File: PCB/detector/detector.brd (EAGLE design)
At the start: 53.3 x 51.7 mm, 36 parts, among them IC1 STM32F042K6T6

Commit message: almost ready
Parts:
- removed +3.3V, +5V: (no value), con-ptr500:AK500/2
- removed D1: 3.3V, diode:SOD80C
- removed JP1: (no value), pinhead:1X03/90
- removed JP2: (no value), pinhead:1X04/90
- removed Q1: (no value), crystal:CTS406
- removed S1: DTSM-3, swtich:DTSM-3
- added BAT1: BAT_3V, battery CR1216:CR1216
- added C18, C23: 100nF, resistor:C0603
- added C19, C20, C21, C22: 22pF, resistor:C0603
- added C24: 1u, rcl:C0603
- added C25: 100p, rcl:C0603
- added C26: 100n, rcl:C0603
- added C27, C28: 1n, rcl:C0603
- added CAN+PWR: 4PIN_3.81_KATOWA, zielone raster 3.81:CON-PHOENIX_3.81-4PIN_KAT
- added CR1: 32,768kHz, crystal_scorpio:IL3X
- added D3_SK1: 5A, diode:DO214AA
- added DA1: SN65HVD230, can_driver:SO08
- added FUSE1: 3A, resistor:R0603
- added L1: 1uH/500mA, rcl:L2012C
- added L2: 10uH/20mA, rcl:L2012C
- added L3, L4: (no value), rcl:L3216C
- added LED1, LED3: zielona, led:CHIP-LED0603
- added LED2: niebieska, led:CHIP-LED0603
- added LED4: czerwona, led:CHIP-LED0603
- added MA_BYC_ACS711_!!: ACS712, acs712:SO08
- added PROGRAMATOR: (no value), pinhead:1X06
- added PRZETWORNICA1: 3.3V, OKI-78SR:TO220
- added R10: 120R*, resistor:R0603
- added R11: 390k, resistor:R0603
- added R12, R13: 10k, resistor:R0603
- added R14, R15, R16: 470R, resistor:R0603
- added TRANSIL1: 3.3V, diode:SMBJ
- added U$2: STM32F072RBT6, STM32F072RBT6:TQFP64
- added U$3: ABM3, crystal_scorpio:ABM3
- added U$6: LC03-6R2G, LC03-6R2 - diody ESD do magistrali:SOIC-8
- added U1: LT5538, DFN-8:DFN-8_3X3
- added U2: B39431B3710U410, SON120P300X300X110-6N:SON120P300X300X110-6N
- added ZW_MASY: (no value), resistor:R0603
- added ZW_ZASILANIA: (no value), pinhead:1X02
- C1: value 100n -> (none); device rcl:C0805 -> rcl:C0603
- C10, C12, C15: value 100n -> 100nF; device rcl:C0805 -> resistor:C0603
- C11, C9: value 4.7u -> 100nF; device rcl:CT3216 -> resistor:C0603
- C13: value 10n -> 100nF; device rcl:C0805 -> resistor:C0603
- C14: value 1u -> 100nF; device rcl:CT3216 -> resistor:C0603
- C16: value 20p -> 100nF; device rcl:C0805 -> resistor:C0603
- C17: value 20p -> 6,3V/100uF; device rcl:C0805 -> resistor:E2-5
- C2: value 100p -> 4,7uF; device rcl:C0805 -> rcl:SMC_A
- C3: value 100p -> (none); device rcl:C0805 -> rcl:C0603
- C4: device rcl:C0805 -> rcl:C0603
- C5, C6: value 100n -> 100p; device rcl:C0805 -> rcl:C0603
- C7: value 10u -> 4,7uF; device rcl:C0805 -> rcl:SMC_A
- C8: value 100n -> 1uF; device rcl:C0805 -> resistor:C0603
- IC1: value STM32F042K6T6 -> LM50; device STM32F042K6T6:QFP80P900X900X160-32N -> linear:SOT23
- R1: value 60.4R -> VARISTORCN0603; device rcl:R0805 -> varistor:CT/CN0603
- R2: value 2k -> (none); device rcl:R0805 -> rcl:R0603
- R3: value 301R -> 820R; device rcl:R0805 -> resistor:R0603
- R4: value 10k -> 56R; device rcl:R0805 -> rcl:R0603
- R5: value 20k -> (none); device rcl:R0805 -> rcl:R0603
- R6: value 1430R -> 10k; device rcl:R0805 -> resistor:R0603
- R7: value 3.74k -> 100K; device rcl:R0805 -> resistor:R0603
- R8: value 2k -> ZW 0-100K; device rcl:R0805 -> resistor:R0603
- R9: value 0R -> 32k; device rcl:R0805 -> resistor:R0603
- U$1: value ADL5902 -> TQP3M9036; device ADL5902:ADL5902 -> DFN-8:DFN-8_2X2
- moved C11 111.4 mm to (127.2, 23.7), flipped to the bottom
- moved C9 101.8 mm to (118.9, 18.9), flipped to the bottom, turned to 90 degrees
- moved C8 100.8 mm to (120.3, 18.9), flipped to the bottom, turned to 90 degrees
- moved C10 99.2 mm to (118.0, 25.9), flipped to the bottom, turned to 180 degrees
- moved C12 98.4 mm to (118.5, 14.5), flipped to the bottom, turned to 0 degrees
- moved R8 97.5 mm to (115.8, 37.9), turned to 270 degrees
- moved C2 95.1 mm to (115.5, 27.3), flipped to the bottom, turned to 0 degrees
- moved C13 89.8 mm to (125.0, 14.5), flipped to the bottom
- moved C7 89.0 mm to (122.0, 19.8), flipped to the bottom
- moved R3 87.3 mm to (111.4, 21.7), turned to 270 degrees
- moved C15 86.5 mm to (115.8, 34.6), turned to 90 degrees
- moved R5 86.2 mm to (117.8, 11.4), turned to 90 degrees
- moved R2 83.9 mm to (108.9, 8.26), turned to 180 degrees
- moved R6 74.6 mm to (99.4, 24.1), flipped to the top, turned to 0 degrees
- moved R7 74.4 mm to (99.4, 22.6)
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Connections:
- net N$1 renamed SIGNAL
- removed net +5V: +5V.1, C3.1, C4.1, C5.1, C6.1, U$1.P$10, U$1.P$3
- removed net ADC_IN: D1.C, IC1.6, R2.1
- removed net INHI: C1.2, U$1.P$14
- removed net OSC_IN: C17.1, IC1.2, Q1.3
- removed net OSC_OUT: C16.1, IC1.3, Q1.1
- removed net RESET: C15.1, IC1.4, JP2.2, S1.1
- removed net SWCLK: IC1.24, JP2.3
- removed net UART_RX: IC1.20, JP1.2
- removed net UART_TX: IC1.19, JP1.3
- removed net VOUT: R4.2, R9.2, U$1.P$6
- new net +24V: C14.1, D3_SK1.C, PRZETWORNICA1.P1
- new net AGND: C18.2, C7.-, C8.2, C9.2, IC1.3, MA_BYC_ACS711_!!.5, R9.1, U$2.12, ZW_MASY.2
- new net AMP_OUT: C27.2, C5.2, R4.2
- new net BOOT_0: PROGRAMATOR.4, R12.2, U$2.60
- new net CANH_1: DA1.7, R10.2, U$6.1
- new net CANL_1: DA1.6, R10.1, U$6.4
- new net CAN_RX_1: DA1.4, U$2.61
- new net CAN_TX_1: DA1.1, U$2.62
- new net DET_OUT: R5.2, U$2.17
- new net FILTER_IN: C3.2, U2.2
- new net FILTER_OUT: C4.1, U2.5
- new net LED1: LED3.A, U$2.11
- new net LED2: LED4.A, U$2.16
- new net N$1: MA_BYC_ACS711_!!.7, R7.1
- new net N$10: C19.1, U$2.5, U$3.P$2
- new net N$11: C4.2, U$1.2
- new net N$12: CAN+PWR.P$2, U$6.8
- new net N$13: R11.1, U$2.4
- new net N$14: C21.1, CR1.P$1, U$2.3
- new net N$15: C22.1, CR1.P$2, R11.2
- new net N$16: CAN+PWR.P$1, U$6.5
- new net N$18: LED1.A, R13.1
- new net N$19: LED2.A, R14.1
- new net N$20: LED3.C, R15.2
- new net N$21: LED4.C, R16.2
- new net N$22: C28.1, U1.3
- new net N$23: C27.1, U1.2
- new net N$24: PROGRAMATOR.2, ZW_ZASILANIA.1
- new net N$25: R2.2, U1.1
- new net N$27: C5.1, L4.2, U$1.7
- new net N$28: U1.7
- new net N$29: U1.6
- new net N$8: D3_SK1.A, MA_BYC_ACS711_!!.1, MA_BYC_ACS711_!!.2
- new net NRST: C23.1, PROGRAMATOR.3, U$2.7
- new net OVER_CURRENT: MA_BYC_ACS711_!!.6, R6.2, U$2.2
- new net PRAD_PLYTKI: R7.2, R9.2, U$2.8
- new net SWD_CLK: PROGRAMATOR.5, U$2.49
- new net TEMP: IC1.2, U$2.9
- new net VBAT: BAT1.P$1, BAT1.P$2, BAT1.P$3, U$2.1
- new net VCC: CAN+PWR.P$4, MA_BYC_ACS711_!!.3, MA_BYC_ACS711_!!.4, R13.2
- new net VDD: C10.1, C11.1, C12.1, C13.1, C15.2, C18.1, C2.+, DA1.3, IC1.1, L1.1, L2.1, MA_BYC_ACS711_!!.8, R6.1, U$2.19, U$2.32, U$2.48, U$2.64, ZW_ZASILANIA.2
- net +3V3: now also C24.1, C25.1, C26.1, C6.1, FUSE1.2, L1.2, L4.1, R14.2, R2.1, TRANSIL1.C, U1.5; no longer +3.3V.1, C10.1, C11.+, C12.1, C13.1, C14.+, C8.1, C9.+, IC1.1, IC1.17, IC1.5
- net GND: now also BAT1.P$4, C11.2, C14.2, C15.1, C17.-, C19.2, C2.-, C20.2, C21.2, C22.2, C23.2, C24.2, C25.2, C26.2, C28.2, CAN+PWR.P$3, DA1.2, L3.2, LED1.C, LED2.C, PROGRAMATOR.1, PRZETWORNICA1.P2, R12.1, R15.1, R16.1, R4.1, R8.2, TRANSIL1.A, U$1.1, U$1.3, U$1.4, U$1.5, U$1.8, U$1.PAD, U$2.18, U$2.31, U$2.47, U$2.63, U$3.P$1, U$3.P$3, U$6.2, U$6.3, U$6.6, U$6.7, U1.4, U1.9, U2.1, U2.3, U2.4, U2.6, ZW_MASY.1; no longer +3.3V.2, +5V.2, C11.-, C14.-, C15.2, C17.2, C2.2, C3.2, C4.2, C5.2, C7.2, C8.2, C9.-, D1.A, IC1.16, IC1.32, JP1.1, JP2.1, R3.1, R5.1, R8.1, S1.2, U$1.P$4, U$1.P$9
- net N$2: now also C16.1, C17.+, FUSE1.1, PRZETWORNICA1.P3; no longer R6.2, R7.2, U$1.P$11
- net N$3: now also R3.1, U$2.6; no longer C2.1, U$1.P$15
- net N$4: now also C7.+, C8.1, C9.1, L2.2, U$2.13; no longer C7.1, U$1.P$5
- net N$5: now also C1.2, C3.1, L3.1; no longer R2.2, R4.1, R5.2
- net N$6: now also C20.1, R3.2, U$3.P$4; no longer R9.1, U$1.P$7
- net N$7: now also DA1.8, R8.1; no longer R3.2, R6.1, U$1.P$1
- net N$9: now also R5.1, U1.8; no longer R7.1, R8.2, U$1.P$12
- net SWDIO: now also PROGRAMATOR.6, U$2.46; no longer IC1.23, JP2.4
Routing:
- net GND: track 20.1 -> 423.6 mm, vias 12 -> 15
- net VDD: track 0.00 -> 101.9 mm, vias 0 -> 9
- net VCC: track 0.00 -> 50.3 mm
- net +5V: track 48.1 -> 0.00 mm, vias 2 -> 0
- net RESET: track 45.8 -> 0.00 mm, vias 2 -> 0
- net AGND: track 0.00 -> 42.5 mm, vias 0 -> 3
- net UART_TX: track 37.7 -> 0.00 mm
- net UART_RX: track 37.0 -> 0.00 mm
- net N$16: track 0.00 -> 31.9 mm
- net N$12: track 0.00 -> 31.3 mm, vias 0 -> 1
- net OVER_CURRENT: track 0.00 -> 30.0 mm, vias 0 -> 2
- net VOUT: track 29.7 -> 0.00 mm
- net +3V3: track 62.7 -> 36.3 mm, vias 0 -> 2
- net NRST: track 0.00 -> 26.4 mm, vias 0 -> 1
- net PRAD_PLYTKI: track 0.00 -> 20.4 mm
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- removed copper zone on layer 1, net GND
- removed copper zone on layer 16, net GND
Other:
- board size 53.3 x 51.7 mm -> 60 x 60 mm
- board text removed: "Detector"
- board text removed: "GND"
- board text removed: "RESET"
- board text removed: "SWCLK"
- board text removed: "SWDIO"
- board text removed: "UART_RX"
- board text removed: "UART_TX"

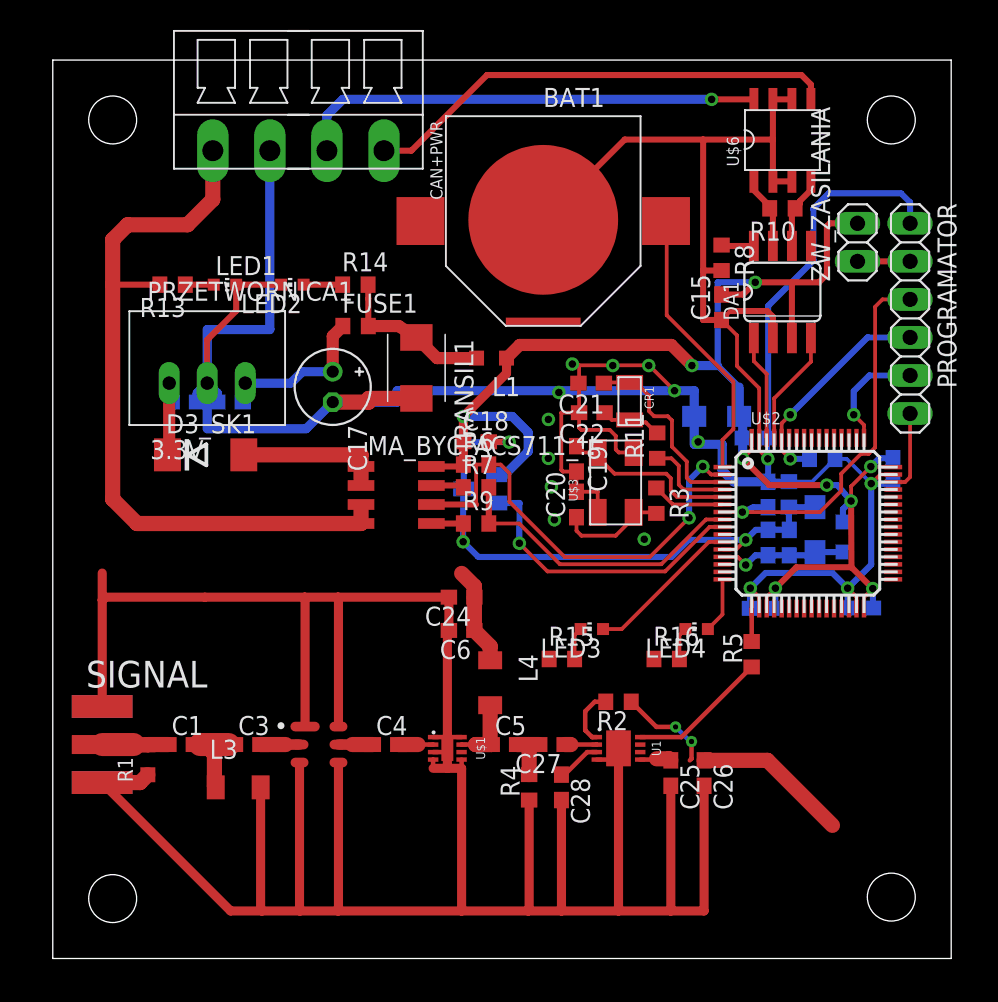
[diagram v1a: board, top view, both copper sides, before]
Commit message: signal gap and vias to add
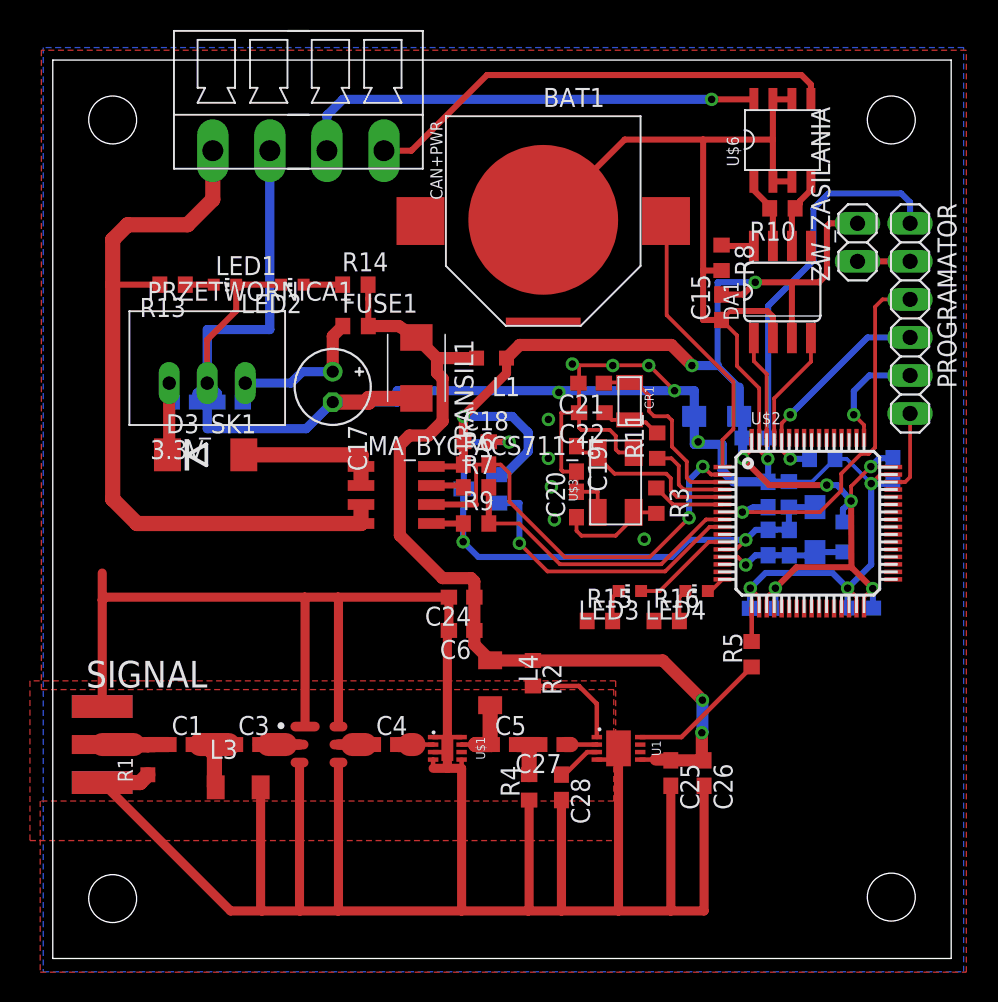
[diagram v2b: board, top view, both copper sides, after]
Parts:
- moved R2 6.02 mm to (103.2, 10.2), turned to 270 degrees
- moved LED3 3.59 mm to (109.7, 15.7)
- moved R15 3.59 mm to (107.7, 13.7)
- moved LED4 2.54 mm to (114.1, 15.7)
- moved R16 2.54 mm to (112.1, 13.7)
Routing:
- net +3V3: track 36.3 -> 60.4 mm
- net LED1: track 10.4 -> 6.79 mm
- net N$25: track 3.87 -> 6.98 mm
- net LED2: track 3.72 -> 1.30 mm
- added copper zone on layer 1, net GND
- added copper zone on layer 16, net GND

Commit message: rf circut edited, pololu lbr added
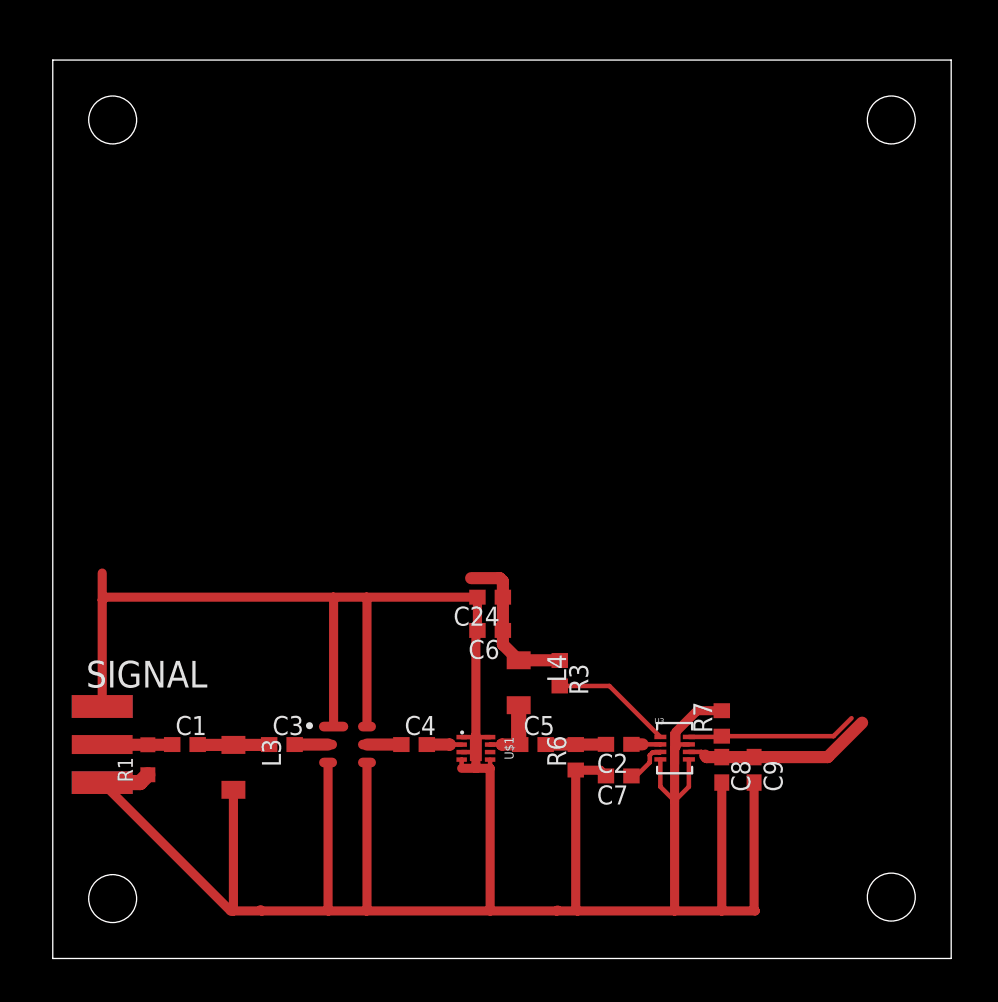
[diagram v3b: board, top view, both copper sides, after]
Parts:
- removed BAT1: BAT_3V, battery CR1216:CR1216
- removed C10, C11, C12, C13, C14, C15, C16, C18, C23: 100nF, resistor:C0603
- removed C17: 6,3V/100uF, resistor:E2-5
- removed C19, C20, C21, C22: 22pF, resistor:C0603
- removed C25: 100p, rcl:C0603
- removed C26: 100n, rcl:C0603
- removed C27, C28: 1n, rcl:C0603
- removed CAN+PWR: 4PIN_3.81_KATOWA, zielone raster 3.81:CON-PHOENIX_3.81-4PIN_KAT
- removed CR1: 32,768kHz, crystal_scorpio:IL3X
- removed D3_SK1: 5A, diode:DO214AA
- removed DA1: SN65HVD230, can_driver:SO08
- removed FUSE1: 3A, resistor:R0603
- removed IC1: LM50, linear:SOT23
- removed L1: 1uH/500mA, rcl:L2012C
- removed L2: 10uH/20mA, rcl:L2012C
- removed LED1, LED3: zielona, led:CHIP-LED0603
- removed LED2: niebieska, led:CHIP-LED0603
- removed LED4: czerwona, led:CHIP-LED0603
- removed MA_BYC_ACS711_!!: ACS712, acs712:SO08
- removed PROGRAMATOR: (no value), pinhead:1X06
- removed PRZETWORNICA1: 3.3V, OKI-78SR:TO220
- removed R10: 120R*, resistor:R0603
- removed R11: 390k, resistor:R0603
- removed R12, R13: 10k, resistor:R0603
- removed R14, R15, R16: 470R, resistor:R0603
- removed R2, R5: (no value), rcl:R0603
- removed R4: 56R, rcl:R0603
- removed R8: ZW 0-100K, resistor:R0603
- removed R9: 32k, resistor:R0603
- removed TRANSIL1: 3.3V, diode:SMBJ
- removed U$2: STM32F072RBT6, STM32F072RBT6:TQFP64
- removed U$3: ABM3, crystal_scorpio:ABM3
- removed U$6: LC03-6R2G, LC03-6R2 - diody ESD do magistrali:SOIC-8
- removed U1: LT5538, DFN-8:DFN-8_3X3
- removed ZW_MASY: (no value), resistor:R0603
- removed ZW_ZASILANIA: (no value), pinhead:1X02
- added U3: LT5537EDDBTRPBF, LT5537EDDBTRPBF:DFN-8_DDB
- C2, C7: value 4,7uF -> 100p; device rcl:SMC_A -> rcl:C0603
- C8: value 1uF -> 1n; device resistor:C0603 -> rcl:C0603
- C9: value 100nF -> 1u; device resistor:C0603 -> rcl:C0603
- R3: value 820R -> (none); device resistor:R0603 -> rcl:R0603
- R6: value 10k -> 51R; device resistor:R0603 -> rcl:R0603
- R7: value 100K -> 33k; device resistor:R0603 -> rcl:R0603
- moved C2 22.9 mm to (108.9, 5.41), flipped to the top, turned to 180 degrees
- moved R7 22.8 mm to (115.8, 6.81), turned to 90 degrees
- moved C7 21.0 mm to (108.9, 3.30), flipped to the top, turned to 180 degrees
- moved R6 20.7 mm to (106.0, 4.55), turned to 90 degrees
- moved C8 15.8 mm to (115.8, 3.71), flipped to the top, turned to 270 degrees
- moved C9 15.2 mm to (118.0, 3.71), flipped to the top, turned to 270 degrees
- moved R3 13.2 mm to (105.0, 10.2)
- moved C3 2.29 mm to (86.4, 5.40)
- moved C24 1.91 mm to (100.3, 15.2)
- moved C4 1.91 mm to (95.2, 5.40)
- moved C5 1.91 mm to (103.2, 5.40)
- moved C6 1.91 mm to (100.3, 13.0)
- moved L4 1.91 mm to (102.2, 9.53)
- moved U$1 1.91 mm to (99.4, 5.14)
- moved U2 1.91 mm to (90.8, 5.40)
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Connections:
- removed net +24V: C14.1, D3_SK1.C, PRZETWORNICA1.P1
- removed net AGND: C18.2, C7.-, C8.2, C9.2, IC1.3, MA_BYC_ACS711_!!.5, R9.1, U$2.12, ZW_MASY.2
- removed net BOOT_0: PROGRAMATOR.4, R12.2, U$2.60
- removed net CANH_1: DA1.7, R10.2, U$6.1
- removed net CANL_1: DA1.6, R10.1, U$6.4
- removed net CAN_RX_1: DA1.4, U$2.61
- removed net CAN_TX_1: DA1.1, U$2.62
- removed net LED1: LED3.A, U$2.11
- removed net LED2: LED4.A, U$2.16
- removed net N$10: C19.1, U$2.5, U$3.P$2
- removed net N$12: CAN+PWR.P$2, U$6.8
- removed net N$13: R11.1, U$2.4
- removed net N$14: C21.1, CR1.P$1, U$2.3
- removed net N$15: C22.1, CR1.P$2, R11.2
- removed net N$16: CAN+PWR.P$1, U$6.5
- removed net N$18: LED1.A, R13.1
- removed net N$19: LED2.A, R14.1
- removed net N$20: LED3.C, R15.2
- removed net N$21: LED4.C, R16.2
- removed net N$22: C28.1, U1.3
- removed net N$23: C27.1, U1.2
- removed net N$24: PROGRAMATOR.2, ZW_ZASILANIA.1
- removed net N$25: R2.2, U1.1
- removed net N$28: U1.7
- removed net N$29: U1.6
- removed net N$4: C7.+, C8.1, C9.1, L2.2, U$2.13
- removed net N$6: C20.1, R3.2, U$3.P$4
- removed net N$7: DA1.8, R8.1
- removed net N$8: D3_SK1.A, MA_BYC_ACS711_!!.1, MA_BYC_ACS711_!!.2
- removed net N$9: R5.1, U1.8
- removed net NRST: C23.1, PROGRAMATOR.3, U$2.7
- removed net OVER_CURRENT: MA_BYC_ACS711_!!.6, R6.2, U$2.2
- removed net PRAD_PLYTKI: R7.2, R9.2, U$2.8
- removed net SWDIO: PROGRAMATOR.6, U$2.46
- removed net SWD_CLK: PROGRAMATOR.5, U$2.49
- removed net TEMP: IC1.2, U$2.9
- removed net VBAT: BAT1.P$1, BAT1.P$2, BAT1.P$3, U$2.1
- removed net VCC: CAN+PWR.P$4, MA_BYC_ACS711_!!.3, MA_BYC_ACS711_!!.4, R13.2
- removed net VDD: C10.1, C11.1, C12.1, C13.1, C15.2, C18.1, C2.+, DA1.3, IC1.1, L1.1, L2.1, MA_BYC_ACS711_!!.8, R6.1, U$2.19, U$2.32, U$2.48, U$2.64, ZW_ZASILANIA.2
- net +3V3: now also C8.1, C9.1, R3.1, U3.6; no longer C25.1, C26.1, FUSE1.2, L1.2, R14.2, R2.1, TRANSIL1.C, U1.5
- net AMP_OUT: now also C2.2, R6.2; no longer C27.2, R4.2
- net DET_OUT: now also R7.1, U3.8; no longer R5.2, U$2.17
- net GND: now also C7.2, C8.2, C9.2, R6.1, R7.2, U3.4, U3.5, U3.7, U3.9; no longer BAT1.P$4, C10.2, C11.2, C12.2, C13.2, C14.2, C15.1, C16.2, C17.-, C19.2, C2.-, C20.2, C21.2, C22.2, C23.2, C25.2, C26.2, C28.2, CAN+PWR.P$3, DA1.2, LED1.C, LED2.C, PROGRAMATOR.1, PRZETWORNICA1.P2, R12.1, R15.1, R16.1, R4.1, R8.2, TRANSIL1.A, U$2.18, U$2.31, U$2.47, U$2.63, U$3.P$1, U$3.P$3, U$6.2, U$6.3, U$6.6, U$6.7, U1.4, U1.9, ZW_MASY.1
- net N$1: now also R3.2, U3.1; no longer MA_BYC_ACS711_!!.7, R7.1
- net N$2: now also C7.1, U3.3; no longer C16.1, C17.+, FUSE1.1, PRZETWORNICA1.P3
- net N$3: now also C2.1, U3.2; no longer R3.1, U$2.6
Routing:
- net GND: track 423.6 -> 208.9 mm, vias 15 -> 0
- net VDD: track 101.9 -> 0.00 mm, vias 9 -> 0
- net VCC: track 50.3 -> 0.00 mm
- net AGND: track 42.5 -> 0.00 mm, vias 3 -> 0
- net +3V3: track 60.4 -> 23.4 mm, vias 2 -> 0
- net N$16: track 31.9 -> 0.00 mm
- net N$12: track 31.3 -> 0.00 mm, vias 1 -> 0
- net OVER_CURRENT: track 30.0 -> 0.00 mm, vias 2 -> 0
- net NRST: track 26.4 -> 0.00 mm, vias 1 -> 0
- net PRAD_PLYTKI: track 20.4 -> 0.00 mm
- net TEMP: track 19.8 -> 0.00 mm, vias 1 -> 0
- net VBAT: track 18.6 -> 0.00 mm
- net BOOT_0: track 14.9 -> 0.00 mm, vias 2 -> 0
- net N$14: track 13.0 -> 0.00 mm
- net N$10: track 11.8 -> 0.00 mm
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- removed copper zone on layer 1, net GND
- removed copper zone on layer 16, net GND

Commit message: reinstall
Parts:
- L3, L4: device rcl:L3216C -> rcl:L2012C
- moved C24 5.54 mm to (97.0, 10.8), turned to 270 degrees
- moved L4 3.19 mm to (102.5, 6.35)
- moved C6 2.47 mm to (99.3, 10.8), turned to 270 degrees
- moved C5 2.41 mm to (105.6, 5.40)
- moved C2 2.29 mm to (111.2, 5.41)
- moved C7 2.29 mm to (111.2, 3.30)
- moved C8 2.29 mm to (118.1, 3.71)
- moved C9 2.29 mm to (120.2, 3.71)
- moved R3 2.29 mm to (107.3, 10.2)
- moved R6 2.29 mm to (108.3, 4.55)
- moved R7 2.29 mm to (118.1, 6.81)
- moved U3 2.29 mm to (114.9, 5.16)
- moved L3 0.51 mm to (83.2, 4.38)
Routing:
- net GND: track 208.9 -> 125.9 mm, vias 0 -> 98
- net +3V3: track 23.4 -> 43.9 mm, vias 0 -> 2
- net N$27: track 4.54 -> 8.97 mm
- net DET_OUT: track 11.4 -> 9.68 mm
- added copper zone on layer 1, net GND
